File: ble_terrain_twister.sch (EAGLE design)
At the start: 14 parts, among them IC1 UA78M33DCY

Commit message: Finished routing. again.
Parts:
- removed BRD1: TERRAIN_TWISTER_EDGEEDGE, terrain_twister_control_board_edge:TERRAIN_TWISTER_EDGEEDGE
- added JP1: (no value), SparkFun:M081.27MM
- added JP2: LEFT_PH, terrain_twister_control_board_edge:LEFT_PH
- added LED1, LED2: LED0603, CEDT:LED0603
- added R1, R2: 100, rcl:R-EU_R0603
- U1: value (none) -> YJ-14015
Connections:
- new net N$1: LED1.C, R1.2
- new net N$2: LED2.C, R2.2
- new net STATUS_LED_A: LED1.A, U1.P0.11
- new net STATUS_LED_B: LED2.A, U1.P0.12
- net A: now also JP1.4; no longer BRD1.A
- net B: now also JP2.7, U1.P0.03/AIN4; no longer BRD1.B, U1.P0.04/AIN5
- net C: now also JP1.7; no longer BRD1.C
- net GND: now also JP1.8, R1.1, R2.1; no longer BRD1.GND
- net M1+: now also JP2.6, U1.P0.02/AIN3; no longer BRD1.M1+, U1.P0.11
- net M1-: now also JP2.5, U1.P0.01/AIN2; no longer BRD1.M1-, U1.P0.12
- net M2+: now also JP1.2; no longer BRD1.M2+
- net M2-: now also JP1.3; no longer BRD1.M2-
- net M3+: now also JP1.5; no longer BRD1.M3+
- net M3-: now also JP1.6; no longer BRD1.M3-
- net SW2: now also JP2.2, U1.P0.00/AREF0; no longer BRD1.SW2, U1.P0.13
- net SW3: now also JP2.1, U1.P0.30; no longer BRD1.SW3, U1.P0.14
- net VBAT: now also JP1.1; no longer BRD1.VBAT
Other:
- note added: "Csak mert van egy csík 0603 zöld LED-em, meg mert egy LED sosem árt!"

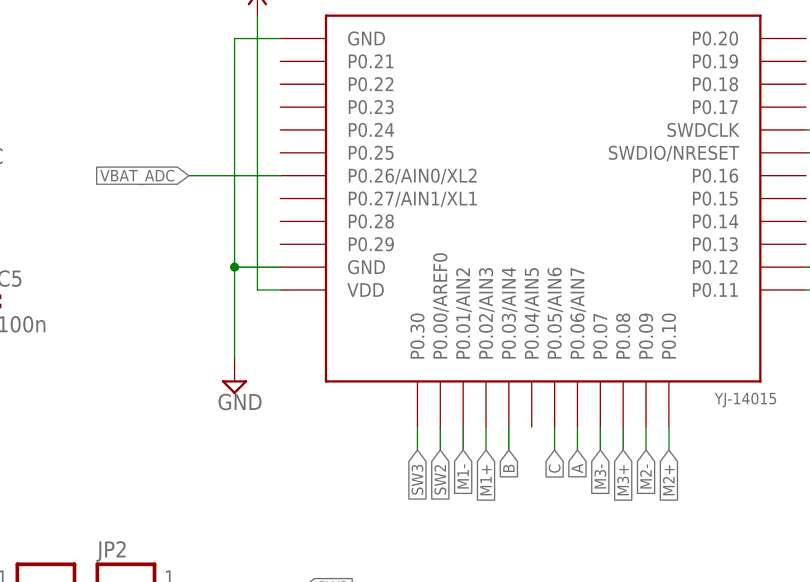
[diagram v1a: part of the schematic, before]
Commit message: YJ-14015 footprint fixed
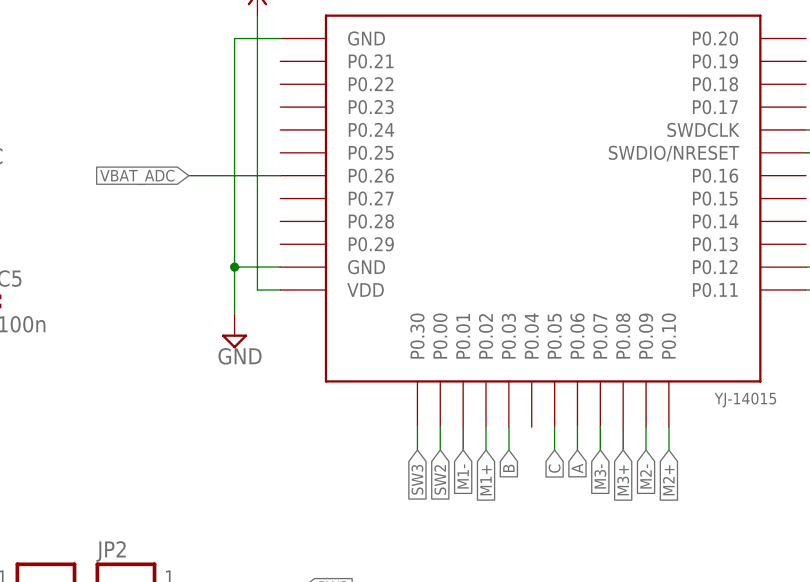
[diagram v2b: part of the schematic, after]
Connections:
- net N$1 renamed LED_A_R
- net N$2 renamed LED_B_R
- net A: now also U1.P0.06; no longer U1.P0.06/AIN7
- net B: now also U1.P0.03; no longer U1.P0.03/AIN4
- net C: now also U1.P0.05; no longer U1.P0.05/AIN6
- net M1+: now also U1.P0.02; no longer U1.P0.02/AIN3
- net M1-: now also U1.P0.01; no longer U1.P0.01/AIN2
- net SW2: now also U1.P0.00; no longer U1.P0.00/AREF0
- net VBAT_ADC: now also U1.P0.26; no longer U1.P0.26/AIN0/XL2
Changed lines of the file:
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@@
 <?xml version="1.0" encoding="utf-8"?>
 <!DOCTYPE eagle SYSTEM "eagle.dtd">
-<eagle version="8.2.1">
+<eagle version="8.3.2">
 <drawing>
 <settings>
 <setting alwaysvectorfont="no"/>
+<setting keepoldvectorfont="yes"/>
 <setting verticaltext="up"/>
 </settings>
@@
 <part name="SWD" library="con-molex" deviceset="53?-04" device="047"/>
 <part name="VCC1" library="logic-supply" deviceset="VCC" device=""/>
-<part name="IC1" library="linear" library_urn="urn:adsk.eagle:library:262" deviceset="UA78M*" device="DCY" technology="33"/>
+<part name="IC1" library="linear" library_urn="urn:adsk.eagle:library:262" deviceset="UA78M*" device="DCY" package3d_urn="urn:adsk.eagle:package:16418/2" technology="33"/>
 <part name="SUPPLY3" library="supply2" deviceset="GND" device=""/>
 <part name="VCC5" library="logic-supply" deviceset="VCC" device=""/>
@@
 <instances>
 <instance part="FRAME1" gate="FRAME" x="0" y="0"/>
-<instance part="U1" gate="YJ-14015" x="119.38" y="127"/>
-<instance part="SUPPLY1" gate="GND" x="83.82" y="104.14"/>
+<instance part="U1" gate="G$1" x="119.38" y="127"/>
+<instance part="SUPPLY1" gate="GND" x="83.82" y="109.22"/>
 <instance part="SUPPLY2" gate="GND" x="48.26" y="58.42"/>
 <instance part="GND3" gate="1" x="215.9" y="111.76"/>
@@
 <net name="GND" class="0">
 <segment>
-<pinref part="U1" gate="YJ-14015" pin="GND@1"/>
+<pinref part="U1" gate="G$1" pin="GND@1"/>
 <pinref part="SUPPLY1" gate="GND" pin="GND"/>
 <wire x1="88.9" y1="116.84" x2="83.82" y2="116.84" width="0.1524" layer="91"/>
-<wire x1="83.82" y1="116.84" x2="83.82" y2="106.68" width="0.1524" layer="91"/>
-<pinref part="U1" gate="YJ-14015" pin="GND@2"/>
+<wire x1="83.82" y1="116.84" x2="83.82" y2="111.76" width="0.1524" layer="91"/>
+<pinref part="U1" gate="G$1" pin="GND@2"/>
 <wire x1="88.9" y1="142.24" x2="83.82" y2="142.24" width="0.1524" layer="91"/>
 <wire x1="83.82" y1="142.24" x2="83.82" y2="116.84" width="0.1524" layer="91"/>
@@
 </segment>
 <segment>
-<pinref part="U1" gate="YJ-14015" pin="VDD"/>
+<pinref part="U1" gate="G$1" pin="VDD"/>
 <pinref part="VCC1" gate="G$1" pin="VCC"/>
 <wire x1="88.9" y1="114.3" x2="86.36" y2="114.3" width="0.1524" layer="91"/>
@@
 </segment>
 <segment>
-<pinref part="U1" gate="YJ-14015" pin="SWDCLK"/>
+<pinref part="U1" gate="G$1" pin="SWDCLK"/>
 <wire x1="147.32" y1="132.08" x2="154.94" y2="132.08" width="0.1524" layer="91"/>
 <label x="154.94" y="132.08" size="1.27" layer="95" font="vector" xref="yes"/>
@@
 </segment>
 <segment>
-<pinref part="U1" gate="YJ-14015" pin="SWDIO/NRESET"/>
+<pinref part="U1" gate="G$1" pin="SWDIO/NRESET"/>
 <wire x1="147.32" y1="129.54" x2="154.94" y2="129.54" width="0.1524" layer="91"/>
 <label x="154.94" y="129.54" size="1.27" layer="95" font="vector" xref="yes"/>
@@
 </segment>
 <segment>
-<pinref part="U1" gate="YJ-14015" pin="P0.30"/>
+<pinref part="U1" gate="G$1" pin="P0.30"/>
 <wire x1="104.14" y1="99.06" x2="104.14" y2="96.52" width="0.1524" layer="91"/>
 <label x="104.14" y="96.52" size="1.27" layer="95" font="vector" rot="R270" xref="yes"/>
@@
 </segment>
 <segment>
-<pinref part="U1" gate="YJ-14015" pin="P0.00/AREF0"/>
+<pinref part="U1" gate="G$1" pin="P0.00"/>
 <wire x1="106.68" y1="99.06" x2="106.68" y2="96.52" width="0.1524" layer="91"/>
 <label x="106.68" y="96.52" size="1.27" layer="95" font="vector" rot="R270" xref="yes"/>
@@
 </segment>
 <segment>
-<pinref part="U1" gate="YJ-14015" pin="P0.26/AIN0/XL2"/>
+<pinref part="U1" gate="G$1" pin="P0.26"/>
 <wire x1="88.9" y1="127" x2="78.74" y2="127" width="0.1524" layer="91"/>
 <label x="78.74" y="127" size="1.27" layer="95" font="vector" rot="R180" xref="yes"/>
@@
 </segment>
 <segment>
-<pinref part="U1" gate="YJ-14015" pin="P0.02/AIN3"/>
+<pinref part="U1" gate="G$1" pin="P0.02"/>
 <wire x1="111.76" y1="99.06" x2="111.76" y2="96.52" width="0.1524" layer="91"/>
 <label x="111.76" y="96.52" size="1.27" layer="95" font="vector" rot="R270" xref="yes"/>
@@
 </segment>
 <segment>
-<pinref part="U1" gate="YJ-14015" pin="P0.01/AIN2"/>
+<pinref part="U1" gate="G$1" pin="P0.01"/>
 <wire x1="109.22" y1="99.06" x2="109.22" y2="96.52" width="0.1524" layer="91"/>
 <label x="109.22" y="96.52" size="1.27" layer="95" font="vector" rot="R270" xref="yes"/>
@@
 </segment>
 <segment>
-<pinref part="U1" gate="YJ-14015" pin="P0.07"/>
+<pinref part="U1" gate="G$1" pin="P0.07"/>
 <wire x1="124.46" y1="99.06" x2="124.46" y2="96.52" width="0.1524" layer="91"/>
 <label x="124.46" y="96.52" size="1.27" layer="95" font="vector" rot="R270" xref="yes"/>
@@
 </segment>
 <segment>
-<pinref part="U1" gate="YJ-14015" pin="P0.08"/>
+<pinref part="U1" gate="G$1" pin="P0.08"/>
 <wire x1="127" y1="99.06" x2="127" y2="96.52" width="0.1524" layer="91"/>
 <label x="127" y="96.52" size="1.27" layer="95" font="vector" rot="R270" xref="yes"/>
@@
 </segment>
 <segment>
-<pinref part="U1" gate="YJ-14015" pin="P0.09"/>
+<pinref part="U1" gate="G$1" pin="P0.09"/>
 <wire x1="129.54" y1="99.06" x2="129.54" y2="96.52" width="0.1524" layer="91"/>
 <label x="129.54" y="96.52" size="1.27" layer="95" font="vector" rot="R270" xref="yes"/>
@@
 </segment>
 <segment>
-<pinref part="U1" gate="YJ-14015" pin="P0.10"/>
+<pinref part="U1" gate="G$1" pin="P0.10"/>
 <wire x1="132.08" y1="99.06" x2="132.08" y2="96.52" width="0.1524" layer="91"/>
 <label x="132.08" y="96.52" size="1.27" layer="95" font="vector" rot="R270" xref="yes"/>
@@
 <net name="A" class="0">
 <segment>
-<pinref part="U1" gate="YJ-14015" pin="P0.06/AIN7"/>
+<pinref part="U1" gate="G$1" pin="P0.06"/>
 <wire x1="121.92" y1="96.52" x2="121.92" y2="99.06" width="0.1524" layer="91"/>
 <label x="121.92" y="96.52" size="1.27" layer="95" font="vector" rot="R270" xref="yes"/>
@@
 <net name="C" class="0">
 <segment>
-<pinref part="U1" gate="YJ-14015" pin="P0.05/AIN6"/>
+<pinref part="U1" gate="G$1" pin="P0.05"/>
 <wire x1="119.38" y1="96.52" x2="119.38" y2="99.06" width="0.1524" layer="91"/>
 <label x="119.38" y="96.52" size="1.27" layer="95" font="vector" rot="R270" xref="yes"/>
@@
 <net name="B" class="0">
 <segment>
-<pinref part="U1" gate="YJ-14015" pin="P0.03/AIN4"/>
+<pinref part="U1" gate="G$1" pin="P0.03"/>
 <wire x1="114.3" y1="99.06" x2="114.3" y2="96.52" width="0.1524" layer="91"/>
 <label x="114.3" y="96.52" size="1.27" layer="95" font="vector" rot="R270" xref="yes"/>
@@
 </segment>
 </net>
-<net name="N$1" class="0">
+<net name="LED_A_R" class="0">
 <segment>
 <pinref part="R1" gate="G$1" pin="2"/>
@@
 </segment>
 </net>
-<net name="N$2" class="0">
+<net name="LED_B_R" class="0">
 <segment>
 <pinref part="R2" gate="G$1" pin="2"/>
@@
 </segment>
 <segment>
-<pinref part="U1" gate="YJ-14015" pin="P0.12"/>
+<pinref part="U1" gate="G$1" pin="P0.12"/>
 <wire x1="147.32" y1="116.84" x2="149.86" y2="116.84" width="0.1524" layer="91"/>
 <label x="149.86" y="116.84" size="1.27" layer="95" font="vector" xref="yes"/>
@@
 </segment>
 <segment>
-<pinref part="U1" gate="YJ-14015" pin="P0.11"/>
+<pinref part="U1" gate="G$1" pin="P0.11"/>
 <wire x1="147.32" y1="114.3" x2="149.86" y2="114.3" width="0.1524" layer="91"/>
 <label x="149.86" y="114.3" size="1.27" layer="95" font="vector" xref="yes"/>
@@
 </note>
 <note version="8.2" severity="warning">
-Since Version 8.2, Eagle supports online libraries. The ids
+Since Version 8.2, EAGLE supports online libraries. The ids
 of those online libraries will not be understood (or retained)
 with this version.
 </note>
+<note version="8.3" severity="warning">
+Since Version 8.3, EAGLE supports URNs for individual library
+assets (packages, symbols, and devices). The URNs of those assets
+will not be understood (or retained) with this version.
+</note>
+<note version="8.3" severity="warning">
+Since Version 8.3, EAGLE supports the association of 3D packages
+with devices in libraries, schematics, and board files. Those 3D
+packages will not be understood (or retained) with this version.
+</note>
 </compatibility>
